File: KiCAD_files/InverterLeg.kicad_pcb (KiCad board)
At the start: 4 copper layers, 29 x 73 mm, 100 parts, among them J801 Conn_Coaxial_Small, J802 Conn_Coaxial_Small, J803 Conn_01x01_Pin, J804 Conn_01x03_Socket, J806 Conn_01x01_Pin, J811 Screw_Terminal_01x01, J814 Screw_Terminal_01x01, J817 Screw_Terminal_01x01, J825 HC-PBB08-2-08-M-H4.0-G1-R-P-04, J827 HC-PBB08-2-08-M-H4.0-G1-R-P-04, J831 HC-PBB08-2-08-M-H4.0-G1-R-P-04, Q801 IPT60R055CM8, Q802 IPT60R055CM8, T801 CMB1670V, T802 CMB1670V, U704 VPS8701B, U707 VPS8701B, U801 LT1761-SD, U802 LT1761-SD, U811 TMP117xxDRV, U815 TMP117xxDRV

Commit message: nearly no problems left with the pcb. still need a little more work
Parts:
- TP801, TP802, TP803, TP804, TP805, TP806, TP807, TP808, TP809, TP810, TP811, TP812, TP813, TP814, TP815, TP816, TP817, TP818, TP819, TP820, TP821, TP822: footprint TestPoint:TestPoint_Pad_D1.0mm -> Footprints:TestPoint_Pad_D1.0mm_small_courtyard
- U603: value ~ -> (none)
- moved TP805 0.16 mm to (136.9, 75.3)
- moved J802 0.14 mm to (140.5, 98.9)
- moved C732 0.12 mm to (134.3, 97.3)
- moved C624 0.10 mm to (157.9, 105.9)
- moved C626 0.10 mm to (152.0, 105.9)
- moved D703 0.09 mm to (137.3, 89.9)
- moved D704 0.09 mm to (134.7, 89.9)
- moved L706 0.09 mm to (134.3, 95.5)
- moved C709 0.08 mm to (138.6, 71.0)
- moved R602 0.06 mm to (146.6, 105.7)
- moved R604 0.06 mm to (141.3, 101.9)
- moved C602 0.06 mm to (152.3, 77.6)
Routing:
- net /ADDR_LS: track 17.2 -> 18.4 mm
- net DGND: track 7.86 -> 7.03 mm, vias 11 -> 12
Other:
- board text added: "DIGITAL"
- board text added: "GND"
- board text added: "POWER"
- board text added: "SWN"
- board text added: "VHIGH"

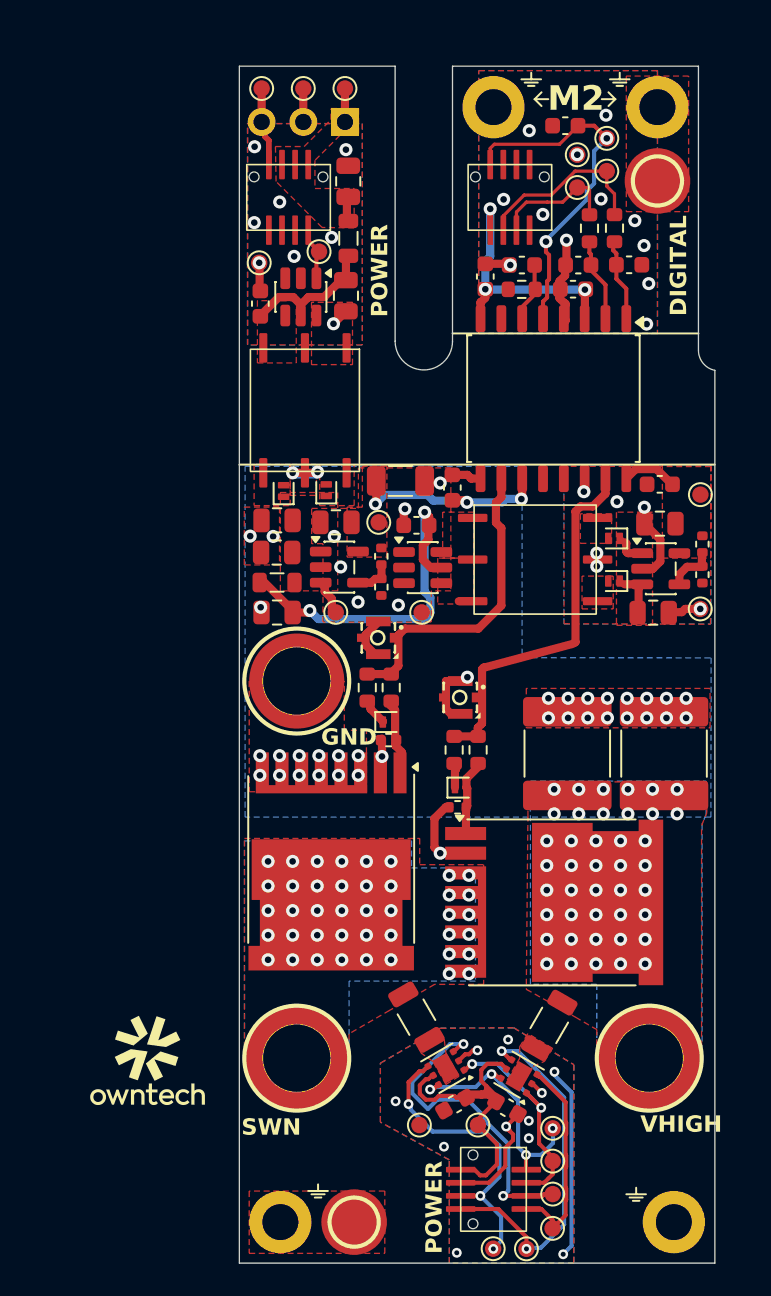
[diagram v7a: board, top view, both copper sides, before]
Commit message: HB board is nearly finished for silicium. need to find the driver and maybe change the MOS. the LCSC number are not done and will be processes after the Driver and mos freeze
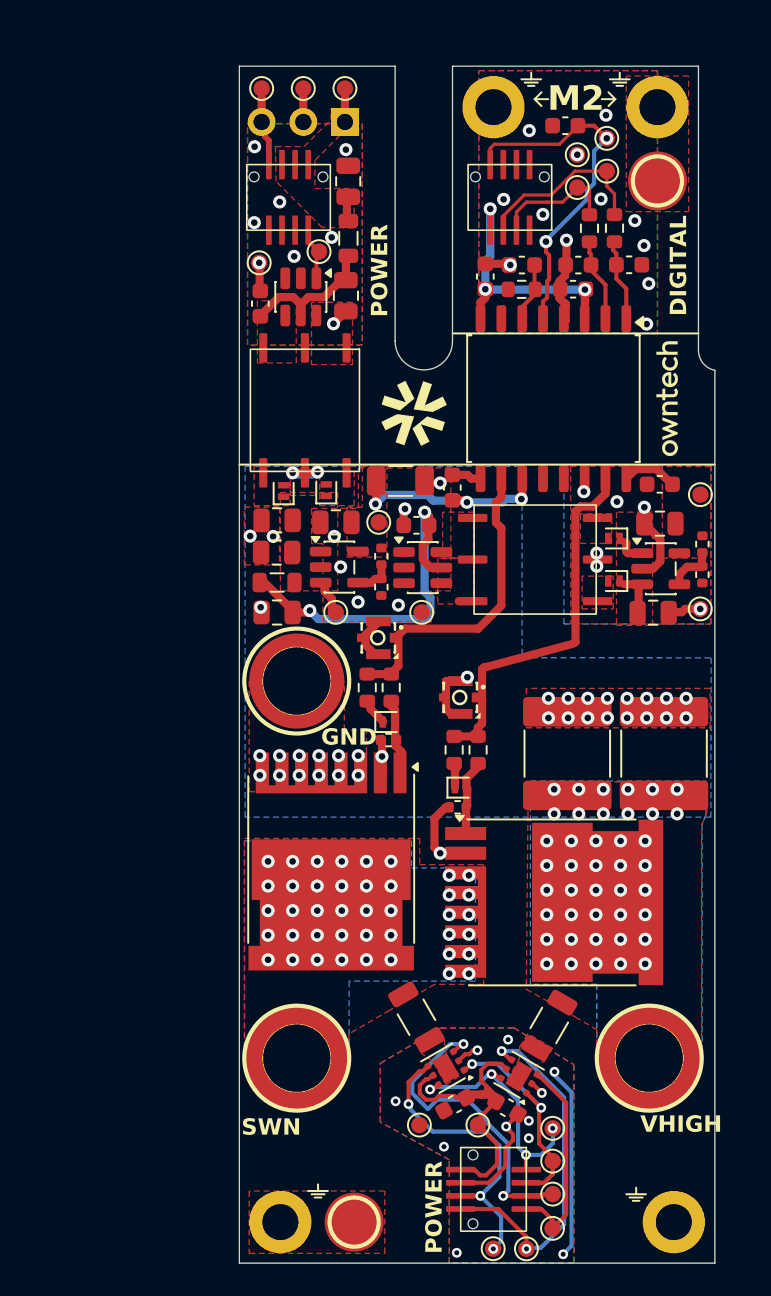
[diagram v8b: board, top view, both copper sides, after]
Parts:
- removed kibuzzard-6A8EFC43: G***, kibuzzard-6A8EFC43
- added kibuzzard-6A9553CF: G***, kibuzzard-6A9553CF, B.Cu at (138.4, 69.9)
- T801, T802: value CMB1670V -> TE1212-2W6ENT
- U603: value (none) -> ~
- moved G*** 53.0 mm to (158.1, 84.3), turned to 90 degrees
- moved G*** 42.0 mm to (142.7, 85.2)
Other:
- board text added: "+12VP"
- board text added: "+5VP"
- board text added: "ADDRHS"
- board text added: "ADDRLS"
- board text added: "ALERTHS"
- board text added: "ALERTLS"
- board text added: "DIS"
- board text added: "EN"
- board text added: "PGND"
- board text added: "PWMH"
- board text added: "PWML"
- board text added: "SCL"
- board text added: "SDA"
- board text added: "SPEED"
- board text added: "x"
